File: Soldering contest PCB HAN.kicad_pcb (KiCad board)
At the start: 2 copper layers, 99 x 99 mm, 11 parts, among them J1 Screw_Terminal_01x02, Q1 2N3904, Q2 2N3904

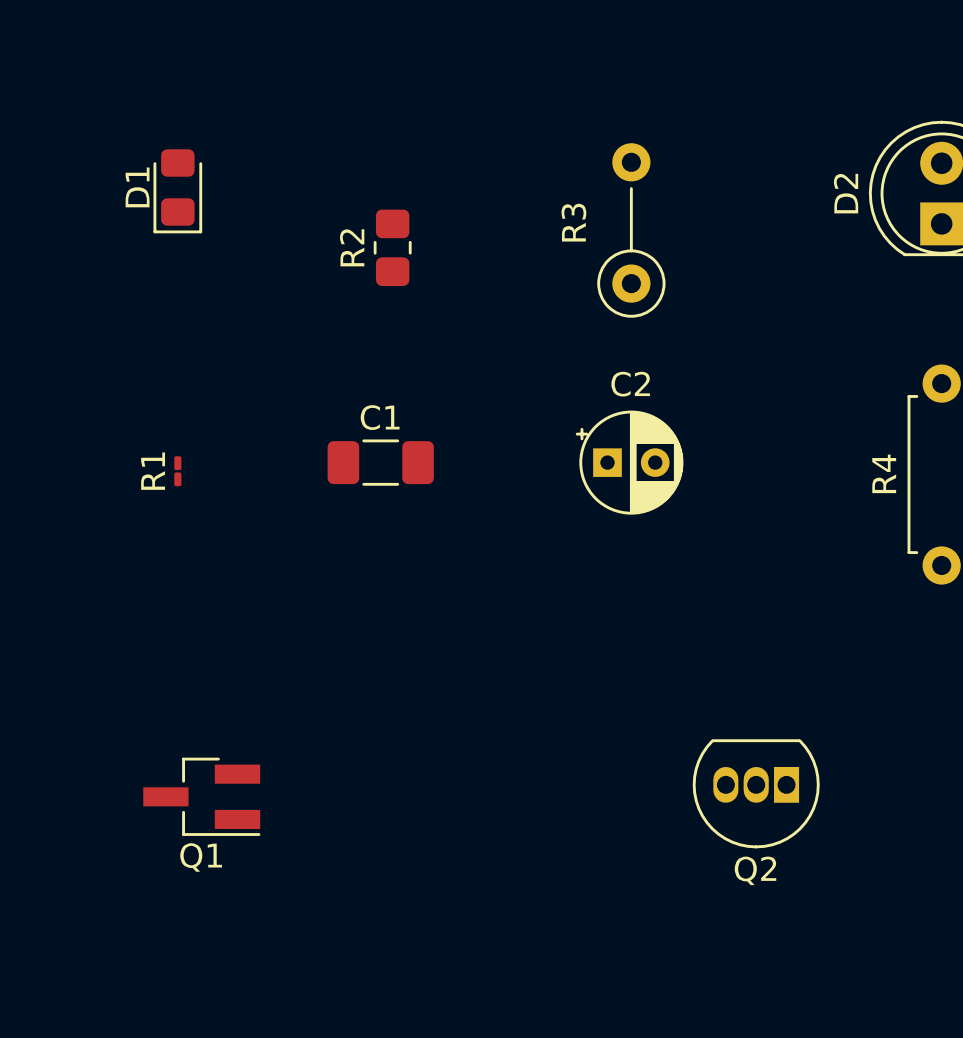
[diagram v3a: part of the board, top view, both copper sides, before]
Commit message: changed r3 footprint
smaller, so it's clear that it has to be soldered vertically
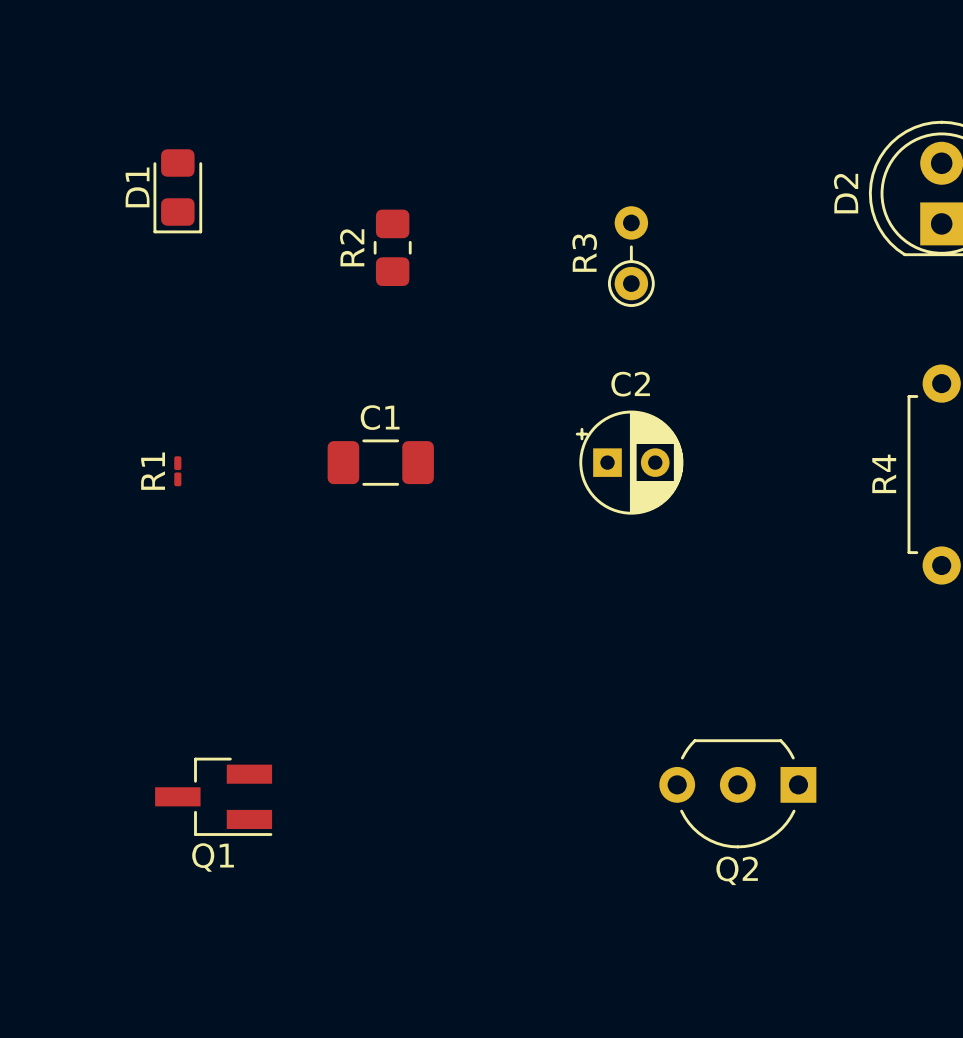
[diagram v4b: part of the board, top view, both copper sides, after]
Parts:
- Q2: footprint Package_TO_SOT_THT:TO-92_Inline -> Package_TO_SOT_THT:TO-92_Inline_Wide
- R3: footprint Resistor_THT:R_Axial_DIN0207_L6.3mm_D2.5mm_P5.08mm_Vertical -> Resistor_THT:R_Axial_DIN0204_L3.6mm_D1.6mm_P2.54mm_Vertical
- moved Q1 0.50 mm to (142.5, 112.0)
- moved Q2 0.50 mm to (167.0, 111.5)
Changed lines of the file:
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@@
     )
   )
-  (footprint "Resistor_THT:R_Axial_DIN0207_L6.3mm_D2.5mm_P5.08mm_Vertical" (layer "F.Cu")
+  (footprint "Resistor_THT:R_Axial_DIN0204_L3.6mm_D1.6mm_P2.54mm_Vertical" (layer "F.Cu")
     (at 160 90.5 90)
-    (descr "Resistor, Axial_DIN0207 series, Axial, Vertical, pin pitch=5.08mm, 0.25W = 1/4W, length*diameter=6.3*2.5mm^2, http://cdn-reichelt.de/documents/datenblatt/B400/1_4W%23YAG.pdf")
-    (tags "Resistor Axial_DIN0207 series Axial Vertical pin pitch 5.08mm 0.25W = 1/4W length 6.3mm diameter 2.5mm")
-    (property "Sheetfile" "Soldering contest PCB HAN.kicad_sch")
-    (property "Sheetname" "")
-    (attr through_hole)
-    (fp_text reference "R3" (at 2.54 -2.37 90) (layer "F.SilkS")
-      (effects (font (size 1 1) (thickness 0.15)))
-    )
-    (fp_text value "10k" (at 2.54 2.37 90) (layer "F.Fab")
-      (effects (font (size 1 1) (thickness 0.15)))
-    )
-    (fp_text user "${REFERENCE}" (at 2.54 -2.37 90) (layer "F.Fab")
-      (effects (font (size 1 1) (thickness 0.15)))
-    )
-    (fp_line (start 1.37 0) (end 3.98 0) (layer "F.SilkS") (width 0.12))
-    (fp_circle (center 0 0) (end 1.37 0) (layer "F.SilkS") (width 0.12) (fill none))
-    (fp_line (start 6.13 -1.5) (end -1.5 -1.5) (layer "F.CrtYd") (width 0.05))
-    (fp_line (start -1.5 -1.5) (end -1.5 1.5) (layer "F.CrtYd") (width 0.05))
-    (fp_line (start -1.5 1.5) (end 6.13 1.5) (layer "F.CrtYd") (width 0.05))
-    (fp_line (start 6.13 1.5) (end 6.13 -1.5) (layer "F.CrtYd") (width 0.05))
-    (fp_line (start 0 0) (end 5.08 0) (layer "F.Fab") (width 0.1))
-    (fp_circle (center 0 0) (end 1.25 0) (layer "F.Fab") (width 0.1) (fill none))
-    (pad "1" thru_hole circle (at 0 0 90) (size 1.6 1.6) (drill 0.8) (layers *.Cu *.Mask)
+    (descr "Resistor, Axial_DIN0204 series, Axial, Vertical, pin pitch=2.54mm, 0.167W, length*diameter=3.6*1.6mm^2, http://cdn-reichelt.de/documents/datenblatt/B400/1_4W%23YAG.pdf")
+    (tags "Resistor Axial_DIN0204 series Axial Vertical pin pitch 2.54mm 0.167W length 3.6mm diameter 1.6mm")
+    (property "Sheetfile" "Soldering contest PCB HAN.kicad_sch")
+    (property "Sheetname" "")
+    (attr through_hole)
+    (fp_text reference "R3" (at 1.27 -1.92 90) (layer "F.SilkS")
+      (effects (font (size 1 1) (thickness 0.15)))
+    )
+    (fp_text value "10k" (at 1.27 1.92 90) (layer "F.Fab")
+      (effects (font (size 1 1) (thickness 0.15)))
+    )
+    (fp_text user "${REFERENCE}" (at 1.27 -1.92 90) (layer "F.Fab")
+      (effects (font (size 1 1) (thickness 0.15)))
+    )
+    (fp_line (start 0.92 0) (end 1.54 0) (layer "F.SilkS") (width 0.12))
+    (fp_circle (center 0 0) (end 0.92 0) (layer "F.SilkS") (width 0.12) (fill none))
+    (fp_line (start -1.05 1.05) (end 3.49 1.05) (layer "F.CrtYd") (width 0.05))
+    (fp_line (start 3.49 -1.05) (end -1.05 -1.05) (layer "F.CrtYd") (width 0.05))
+    (fp_line (start -1.05 -1.05) (end -1.05 1.05) (layer "F.CrtYd") (width 0.05))
+    (fp_line (start 3.49 1.05) (end 3.49 -1.05) (layer "F.CrtYd") (width 0.05))
+    (fp_line (start 0 0) (end 2.54 0) (layer "F.Fab") (width 0.1))
+    (fp_circle (center 0 0) (end 0.8 0) (layer "F.Fab") (width 0.1) (fill none))
+    (pad "1" thru_hole circle (at 0 0 90) (size 1.4 1.4) (drill 0.7) (layers *.Cu *.Mask)
       (net 6 "Net-(D1-Pad2)") (pintype "passive"))
-    (pad "2" thru_hole oval (at 5.08 0 90) (size 1.6 1.6) (drill 0.8) (layers *.Cu *.Mask)
+    (pad "2" thru_hole oval (at 2.54 0 90) (size 1.4 1.4) (drill 0.7) (layers *.Cu *.Mask)
       (net 4 "Net-(C2-Pad2)") (pintype "passive"))
-    (model "${KIPRJMOD}/packages3D/R_Axial_DIN0207_L6.3mm_D2.5mm_P5.08mm_Vertical.wrl"
+    (model "${KICAD6_3DMODEL_DIR}/Resistor_THT.3dshapes/R_Axial_DIN0204_L3.6mm_D1.6mm_P2.54mm_Vertical.wrl"
       (offset (xyz 0 0 0))
       (scale (xyz 1 1 1))
@@
   )
   (footprint "Package_TO_SOT_SMD:SOT-23_Handsoldering" (layer "F.Cu")
-    (at 142 112 180)
+    (at 142.5 112 180)
     (descr "SOT-23, Handsoldering")
     (tags "SOT-23")
@@
     )
   )
-  (footprint "Package_TO_SOT_THT:TO-92_Inline" (layer "F.Cu")
-    (at 166.5 111.5 180)
-    (descr "TO-92 leads in-line, narrow, oval pads, drill 0.75mm (see NXP sot054_po.pdf)")
+  (footprint "Package_TO_SOT_THT:TO-92_Inline_Wide" (layer "F.Cu")
+    (at 167 111.5 180)
+    (descr "TO-92 leads in-line, wide, drill 0.75mm (see NXP sot054_po.pdf)")
     (tags "to-92 sc-43 sc-43a sot54 PA33 transistor")
     (property "Sheetfile" "Soldering contest PCB HAN.kicad_sch")
     (property "Sheetname" "")
     (attr through_hole)
-    (fp_text reference "Q2" (at 1.27 -3.56) (layer "F.SilkS")
-      (effects (font (size 1 1) (thickness 0.15)))
-    )
-    (fp_text value "2N3904" (at 1.27 2.79) (layer "F.Fab")
-      (effects (font (size 1 1) (thickness 0.15)))
-    )
-    (fp_text user "${REFERENCE}" (at 1.27 0) (layer "F.Fab")
-      (effects (font (size 1 1) (thickness 0.15)))
-    )
-    (fp_line (start -0.53 1.85) (end 3.07 1.85) (layer "F.SilkS") (width 0.12))
-    (fp_arc (start 1.27 -2.6) (mid 3.672087 -0.994977) (end 3.108478 1.838478) (layer "F.SilkS") (width 0.12))
-    (fp_arc (start -0.568478 1.838478) (mid -1.132087 -0.994977) (end 1.27 -2.6) (layer "F.SilkS") (width 0.12))
-    (fp_line (start -1.46 -2.73) (end -1.46 2.01) (layer "F.CrtYd") (width 0.05))
-    (fp_line (start 4 2.01) (end 4 -2.73) (layer "F.CrtYd") (width 0.05))
-    (fp_line (start -1.46 -2.73) (end 4 -2.73) (layer "F.CrtYd") (width 0.05))
-    (fp_line (start 4 2.01) (end -1.46 2.01) (layer "F.CrtYd") (width 0.05))
-    (fp_line (start -0.5 1.75) (end 3 1.75) (layer "F.Fab") (width 0.1))
-    (fp_arc (start 1.27 -2.48) (mid 3.561221 -0.949055) (end 3.023625 1.753625) (layer "F.Fab") (width 0.1))
-    (fp_arc (start -0.483625 1.753625) (mid -1.021221 -0.949055) (end 1.27 -2.48) (layer "F.Fab") (width 0.1))
-    (pad "1" thru_hole rect (at 0 0 180) (size 1.05 1.5) (drill 0.75) (layers *.Cu *.Mask)
+    (fp_text reference "Q2" (at 2.54 -3.56 180) (layer "F.SilkS")
+      (effects (font (size 1 1) (thickness 0.15)))
+    )
+    (fp_text value "2N3904" (at 2.54 2.79 180) (layer "F.Fab")
+      (effects (font (size 1 1) (thickness 0.15)))
+    )
+    (fp_text user "${REFERENCE}" (at 2.54 0 180) (layer "F.Fab")
+      (effects (font (size 1 1) (thickness 0.15)))
+    )
+    (fp_line (start 0.74 1.85) (end 4.34 1.85) (layer "F.SilkS") (width 0.12))
+    (fp_arc (start 0.1836 -1.098807) (mid 1.143021 -2.192817) (end 2.54 -2.6) (layer "F.SilkS") (width 0.12))
+    (fp_arc (start 2.54 -2.6) (mid 3.936979 -2.192818) (end 4.8964 -1.098807) (layer "F.SilkS") (width 0.12))
+    (fp_arc (start 4.864184 1.122795) (mid 4.633903 1.509328) (end 4.34 1.85) (layer "F.SilkS") (width 0.12))
+    (fp_arc (start 0.74 1.85) (mid 0.446097 1.509328) (end 0.215816 1.122795) (layer "F.SilkS") (width 0.12))
+    (fp_line (start -1.01 -2.73) (end -1.01 2.01) (layer "F.CrtYd") (width 0.05))
+    (fp_line (start 6.09 2.01) (end -1.01 2.01) (layer "F.CrtYd") (width 0.05))
+    (fp_line (start -1.01 -2.73) (end 6.09 -2.73) (layer "F.CrtYd") (width 0.05))
+    (fp_line (start 6.09 2.01) (end 6.09 -2.73) (layer "F.CrtYd") (width 0.05))
+    (fp_line (start 0.8 1.75) (end 4.3 1.75) (layer "F.Fab") (width 0.1))
+    (fp_arc (start 0.786375 1.753625) (mid 0.248779 -0.949055) (end 2.54 -2.48) (layer "F.Fab") (width 0.1))
+    (fp_arc (start 2.54 -2.48) (mid 4.831221 -0.949055) (end 4.293625 1.753625) (layer "F.Fab") (width 0.1))
+    (pad "1" thru_hole rect (at 0 0 180) (size 1.5 1.5) (drill 0.8) (layers *.Cu *.Mask)
       (net 8 "GND") (pinfunction "E") (pintype "passive"))
-    (pad "2" thru_hole oval (at 1.27 0 180) (size 1.05 1.5) (drill 0.75) (layers *.Cu *.Mask)
+    (pad "2" thru_hole circle (at 2.54 0 180) (size 1.5 1.5) (drill 0.8) (layers *.Cu *.Mask)
       (net 2 "Net-(C1-Pad2)") (pinfunction "B") (pintype "passive"))
-    (pad "3" thru_hole oval (at 2.54 0 180) (size 1.05 1.5) (drill 0.75) (layers *.Cu *.Mask)
+    (pad "3" thru_hole circle (at 5.08 0 180) (size 1.5 1.5) (drill 0.8) (layers *.Cu *.Mask)
       (net 3 "Net-(C2-Pad1)") (pinfunction "C") (pintype "passive"))
-    (model "${KIPRJMOD}/packages3D/TO-92_Inline.wrl"
-      (offset (xyz 0 0 0))
-      (scale (xyz 1 1 1))
+    (model "${KICAD6_3DMODEL_DIR}/Package_TO_SOT_THT.3dshapes/TO-92_Inline_Wide.wrl"
+      (offset (xyz 0 0 0))
+      (scale (xyz 1 1 1))

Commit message: Wiring complete
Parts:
- moved R3 2.50 mm to (160.0, 88.0), turned to -90 degrees
- turned R2 to -90 degrees
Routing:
- net Net-(C2-Pad2): track 0.00 -> 107.4 mm
- net Net-(D1-Pad2): track 0.00 -> 65.9 mm
- net GND: track 0.00 -> 56.2 mm
- net Net-(C1-Pad2): track 0.00 -> 35.8 mm
- net Net-(C2-Pad1): track 0.00 -> 25.6 mm
- net Net-(C1-Pad1): track 0.00 -> 20.5 mm
- net Net-(D1-Pad1): track 0.00 -> 10.5 mm
- net Net-(D2-Pad1): track 0.00 -> 6.69 mm
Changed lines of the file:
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@@
   (net 8 "GND")
   (footprint "Resistor_SMD:R_0805_2012Metric_Pad1.20x1.40mm_HandSolder" (layer "F.Cu")
-    (at 150 89 90)
+    (at 150 89 -90)
     (descr "Resistor SMD 0805 (2012 Metric), square (rectangular) end terminal, IPC_7351 nominal with elongated pad for handsoldering. (Body size source: IPC-SM-782 page 72, https://www.pcb-3d.com/wordpress/wp-content/uploads/ipc-sm-782a_amendment_1_and_2.pdf), generated with kicad-footprint-generator")
     (tags "resistor handsolder")
@@
     (fp_line (start -1 -0.625) (end 1 -0.625) (layer "F.Fab") (width 0.1))
     (fp_line (start -1 0.625) (end -1 -0.625) (layer "F.Fab") (width 0.1))
-    (pad "1" smd roundrect (at -1 0 90) (size 1.2 1.4) (layers "F.Cu" "F.Paste" "F.Mask") (roundrect_rratio 0.208333)
+    (pad "1" smd roundrect (at -1 0 270) (size 1.2 1.4) (layers "F.Cu" "F.Paste" "F.Mask") (roundrect_rratio 0.208333)
       (net 6 "Net-(D1-Pad2)") (pintype "passive"))
-    (pad "2" smd roundrect (at 1 0 90) (size 1.2 1.4) (layers "F.Cu" "F.Paste" "F.Mask") (roundrect_rratio 0.208333)
+    (pad "2" smd roundrect (at 1 0 270) (size 1.2 1.4) (layers "F.Cu" "F.Paste" "F.Mask") (roundrect_rratio 0.208333)
       (net 2 "Net-(C1-Pad2)") (pintype "passive"))
     (model "${KIPRJMOD}/packages3D/R_0805_2012Metric.wrl"
@@
   )
   (footprint "Resistor_THT:R_Axial_DIN0204_L3.6mm_D1.6mm_P2.54mm_Vertical" (layer "F.Cu")
-    (at 160 90.5 90)
+    (at 160 88 -90)
     (descr "Resistor, Axial_DIN0204 series, Axial, Vertical, pin pitch=2.54mm, 0.167W, length*diameter=3.6*1.6mm^2, http://cdn-reichelt.de/documents/datenblatt/B400/1_4W%23YAG.pdf")
     (tags "Resistor Axial_DIN0204 series Axial Vertical pin pitch 2.54mm 0.167W length 3.6mm diameter 1.6mm")
@@
     (fp_line (start 0 0) (end 2.54 0) (layer "F.Fab") (width 0.1))
     (fp_circle (center 0 0) (end 0.8 0) (layer "F.Fab") (width 0.1) (fill none))
-    (pad "1" thru_hole circle (at 0 0 90) (size 1.4 1.4) (drill 0.7) (layers *.Cu *.Mask)
+    (pad "1" thru_hole circle (at 0 0 270) (size 1.4 1.4) (drill 0.7) (layers *.Cu *.Mask)
       (net 6 "Net-(D1-Pad2)") (pintype "passive"))
-    (pad "2" thru_hole oval (at 2.54 0 90) (size 1.4 1.4) (drill 0.7) (layers *.Cu *.Mask)
+    (pad "2" thru_hole oval (at 2.54 0 270) (size 1.4 1.4) (drill 0.7) (layers *.Cu *.Mask)
       (net 4 "Net-(C2-Pad2)") (pintype "passive"))
     (model "${KICAD6_3DMODEL_DIR}/Resistor_THT.3dshapes/R_Axial_DIN0204_L3.6mm_D1.6mm_P2.54mm_Vertical.wrl"
@@
   )
   (gr_rect (start 111.5 51) (end 210.5 150) (layer "Edge.Cuts") (width 0.2) (fill none))
+  (segment (start 144.3 98.7) (end 141 98.7) (width 0.25) (layer "F.Cu") (net 1))
+  (segment (start 145 98) (end 144.3 98.7) (width 0.25) (layer "F.Cu") (net 1))
+  (segment (start 141 112) (end 141 98.7) (width 0.25) (layer "F.Cu") (net 1))
+  (segment (start 147.9375 98) (end 145 98) (width 0.25) (layer "F.Cu") (net 1))
+  (segment (start 164.46 113.04) (end 163 114.5) (width 0.25) (layer "F.Cu") (net 2))
+  (segment (start 150 90) (end 151 91) (width 0.25) (layer "F.Cu") (net 2))
+  (segment (start 151 97.9375) (end 151.0625 98) (width 0.25) (layer "F.Cu") (net 2))
+  (segment (start 151 91) (end 151 97.9375) (width 0.25) (layer "F.Cu") (net 2))
+  (segment (start 159 114.5) (end 151.0625 106.5625) (width 0.25) (layer "F.Cu") (net 2))
+  (segment (start 164.46 111.5) (end 164.46 113.04) (width 0.25) (layer "F.Cu") (net 2))
+  (segment (start 163 114.5) (end 159 114.5) (width 0.25) (layer "F.Cu") (net 2))
+  (segment (start 151.0625 106.5625) (end 151.0625 98) (width 0.25) (layer "F.Cu") (net 2))
+  (segment (start 161.92 100.92) (end 159 98) (width 0.25) (layer "F.Cu") (net 3))
+  (segment (start 163.5 109.92) (end 163.5 102.5) (width 0.25) (layer "F.Cu") (net 3))
+  (segment (start 173 102.31) (end 172.81 102.5) (width 0.25) (layer "F.Cu") (net 3))
+  (segment (start 172.81 102.5) (end 163.5 102.5) (width 0.25) (layer "F.Cu") (net 3))
+  (segment (start 163.5 102.5) (end 161.92 100.92) (width 0.25) (layer "F.Cu") (net 3))
+  (segment (start 161.92 111.5) (end 163.5 109.92) (width 0.25) (layer "F.Cu") (net 3))
+  (segment (start 184 97) (end 169 112) (width 0.25) (layer "F.Cu") (net 4))
+  (segment (start 166 117.5) (end 145 117.5) (width 0.25) (layer "F.Cu") (net 4))
+  (segment (start 161 98) (end 178 98) (width 0.25) (layer "F.Cu") (net 4))
+  (segment (start 190.5 93) (end 190.5 95.5) (width 0.25) (layer "F.Cu") (net 4))
+  (segment (start 169 112) (end 169 114.5) (width 0.25) (layer "F.Cu") (net 4))
+  (segment (start 145 117.5) (end 142.5 115) (width 0.25) (layer "F.Cu") (net 4))
+  (segment (start 178 98) (end 184.5 91.5) (width 0.25) (layer "F.Cu") (net 4))
+  (segment (start 190.5 95.5) (end 189 97) (width 0.25) (layer "F.Cu") (net 4))
+  (segment (start 142.5 112.5) (end 143.95 111.05) (width 0.25) (layer "F.Cu") (net 4))
+  (segment (start 143.95 111.05) (end 144 111.05) (width 0.25) (layer "F.Cu") (net 4))
+  (segment (start 169 114.5) (end 166 117.5) (width 0.25) (layer "F.Cu") (net 4))
+  (segment (start 160 90.54) (end 160 97) (width 0.25) (layer "F.Cu") (net 4))
+  (segment (start 160 97) (end 161 98) (width 0.25) (layer "F.Cu") (net 4))
+  (segment (start 189 91.5) (end 190.5 93) (width 0.25) (layer "F.Cu") (net 4))
+  (segment (start 184.5 91.5) (end 189 91.5) (width 0.25) (layer "F.Cu") (net 4))
+  (segment (start 189 97) (end 184 97) (width 0.25) (layer "F.Cu") (net 4))
+  (segment (start 142.5 115) (end 142.5 112.5) (width 0.25) (layer "F.Cu") (net 4))
+  (segment (start 141 98.025) (end 141 87.5) (width 0.25) (layer "F.Cu") (net 5))
+  (segment (start 150 88) (end 160 88) (width 0.25) (layer "F.Cu") (net 6))
+  (segment (start 162.54 85.46) (end 160 88) (width 0.25) (layer "F.Cu") (net 6))
+  (segment (start 173 85.46) (end 185.96 85.46) (width 0.25) (layer "F.Cu") (net 6))
+  (segment (start 189 99.5) (end 187.5 99.5) (width 0.25) (layer "F.Cu") (net 6))
+  (segment (start 173 85.46) (end 162.54 85.46) (width 0.25) (layer "F.Cu") (net 6))
+  (segment (start 147.5 88) (end 150 88) (width 0.25) (layer "F.Cu") (net 6))
+  (segment (start 191.5 97) (end 189 99.5) (width 0.25) (layer "F.Cu") (net 6))
+  (segment (start 185.96 85.46) (end 191.5 91) (width 0.25) (layer "F.Cu") (net 6))
+  (segment (start 144.95 85.45) (end 147.5 88) (width 0.25) (layer "F.Cu") (net 6))
+  (segment (start 191.5 91) (end 191.5 97) (width 0.25) (layer "F.Cu") (net 6))
+  (segment (start 141 85.45) (end 144.95 85.45) (width 0.25) (layer "F.Cu") (net 6))
+  (segment (start 173 94.69) (end 173 88) (width 0.25) (layer "F.Cu") (net 7))
+  (segment (start 167 114.5) (end 165 116.5) (width 0.25) (layer "F.Cu") (net 8))
+  (segment (start 184.08 94.42) (end 167 111.5) (width 0.25) (layer "F.Cu") (net 8))
+  (segment (start 167 111.5) (end 167 114.5) (width 0.25) (layer "F.Cu") (net 8))
+  (segment (start 144 113.5) (end 144 112.95) (width 0.25) (layer "F.Cu") (net 8))
+  (segment (start 147 116.5) (end 144 113.5) (width 0.25) (layer "F.Cu") (net 8))
+  (segment (start 187.5 94.42) (end 184.08 94.42) (width 0.25) (layer "F.Cu") (net 8))
+  (segment (start 165 116.5) (end 147 116.5) (width 0.25) (layer "F.Cu") (net 8))
 )
